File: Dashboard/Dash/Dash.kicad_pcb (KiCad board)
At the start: 2 copper layers, 184 x 75 mm, 44 parts, among them IC1 MCP25625-E_SS, J1 TACH-SERVO, J2 SPEED-SERVO, J4 UPPER Button, J6 LOWER Button, J7 DTF13-6P, U1 XIAO-ESP32-S3-SMD, U3 EA DOGM128W-6, Y1 ABM10AIG-16.000MHZ-4Z-T3

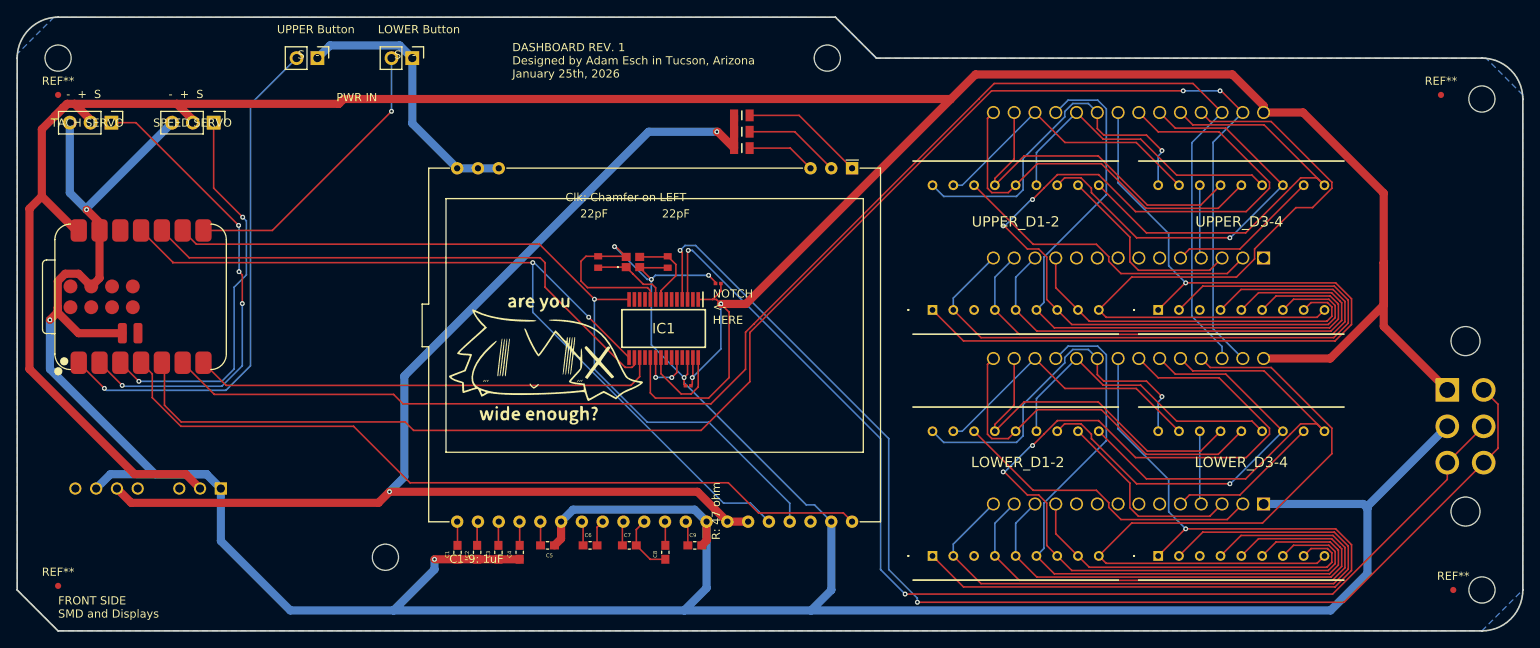
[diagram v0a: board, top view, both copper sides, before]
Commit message: Swapped upper button for CAN_INT
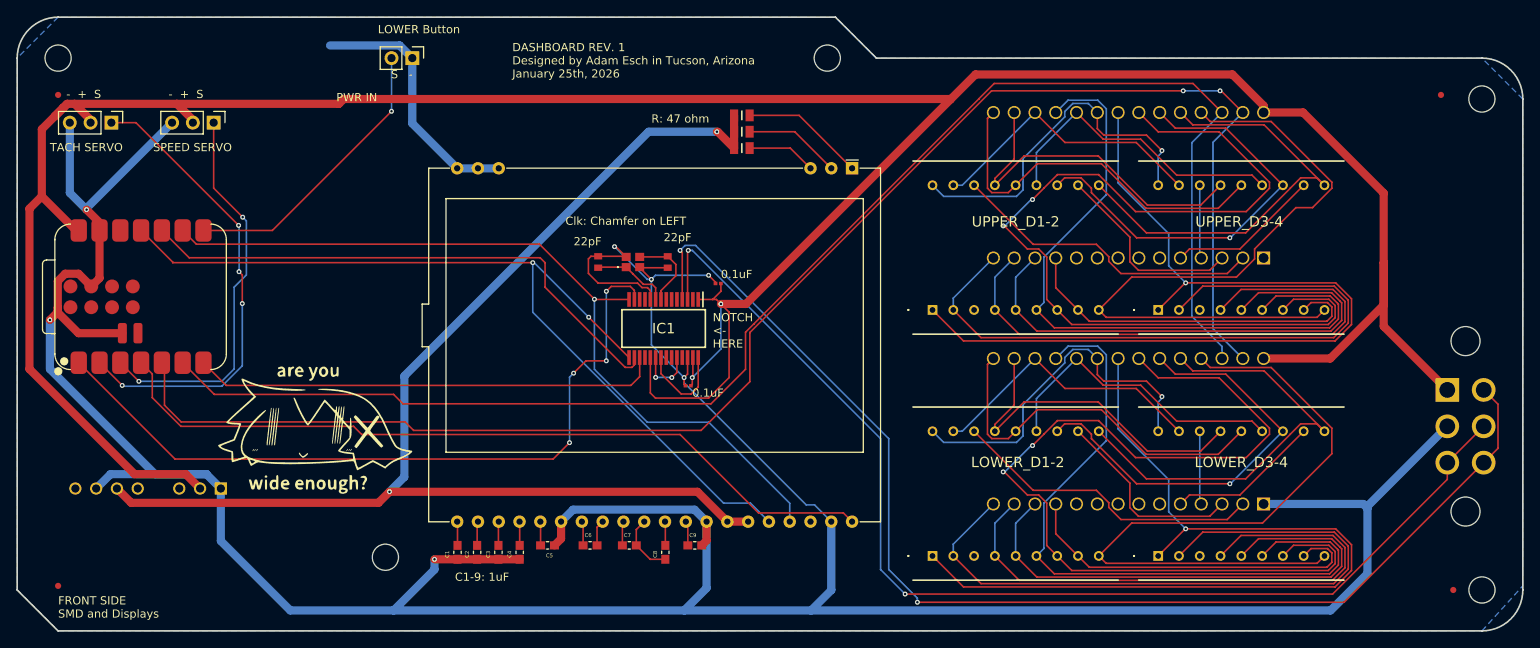
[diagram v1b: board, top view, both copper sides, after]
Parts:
- removed J4: UPPER Button, Connector_PinHeader_2.54mm:PinHeader_1x02_P2.54mm_Vertical
- moved G*** 29.4 mm to (86.0, 108.5)
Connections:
- IC1 pad 13: unconnected-(IC1-~{INT}-Pad13) -> CAN_INT
- U1 pad 1: UPPER_Button -> CAN_INT
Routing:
- net CAN_INT: track 0.00 -> 92.5 mm, vias 0 -> 4
- net UPPER_Button: track 63.6 -> 0.00 mm, vias 1 -> 0
- net GND: track 475.6 -> 471.2 mm
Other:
- board text added: "0.1uF"
- board text removed: "UPPER Button"

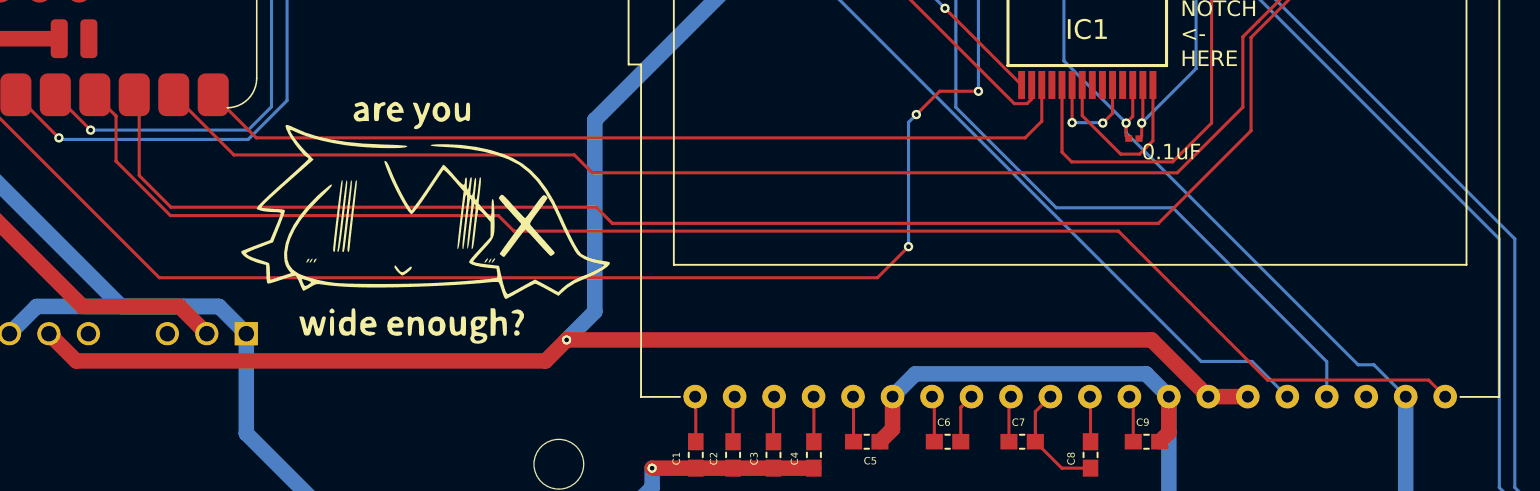
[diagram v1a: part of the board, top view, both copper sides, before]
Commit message: Cleanup on SPI/I2C Traces
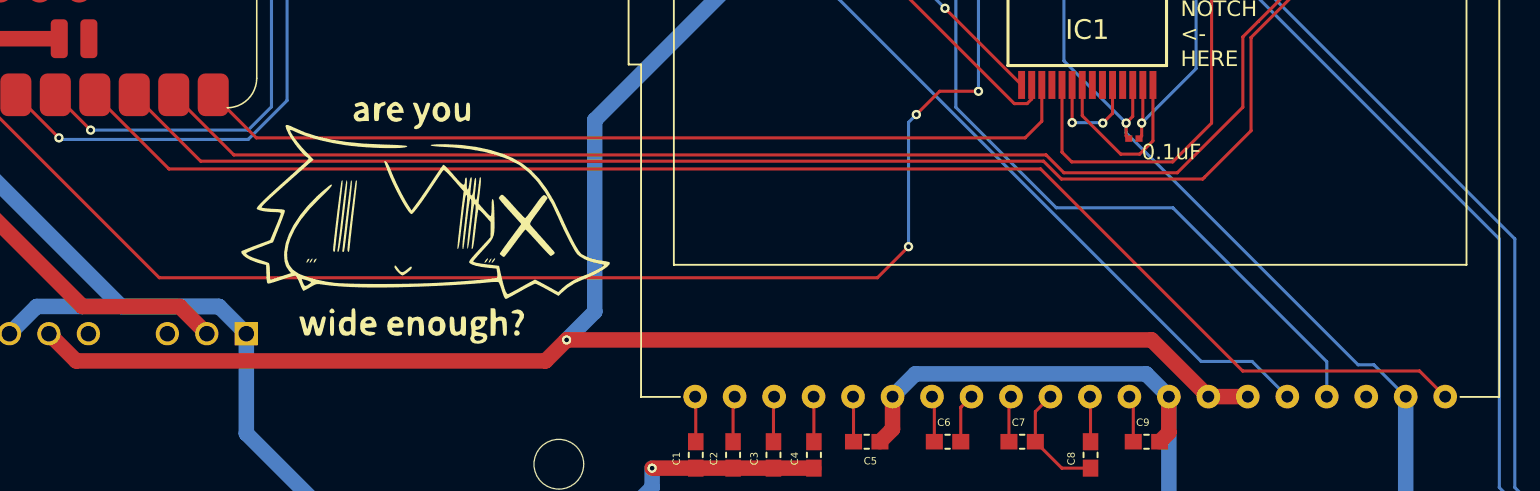
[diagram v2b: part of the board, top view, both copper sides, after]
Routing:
- net SDA: track 192.8 -> 188.0 mm
- net LCD_CS: track 96.6 -> 94.9 mm
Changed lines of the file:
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@@
 			(outputformat 1)
 			(mirror no)
-			(drillshape 1)
+			(drillshape 0)
 			(scaleselection 1)
 			(outputdirectory "")
@@
 	)
 	(segment
-		(start 169.399 66.101)
-		(end 193.693481 66.101)
+		(start 140.010481 95.502)
+		(end 167.510481 68.002)
 		(width 0.2)
 		(layer "F.Cu")
@@
 	)
 	(segment
-		(start 139.010481 101.026817)
-		(end 139.010481 96.5)
+		(start 127.5 105.246609)
+		(end 134.790689 105.246609)
 		(width 0.2)
 		(layer "F.Cu")
@@
 	)
 	(segment
-		(start 97.149057 105.246609)
-		(end 134.790689 105.246609)
+		(start 70.222481 100.228729)
+		(end 74.091304 104.097552)
 		(width 0.2)
 		(layer "F.Cu")
@@
 	)
 	(segment
-		(start 140.008481 95.502)
-		(end 140.010481 95.502)
+		(start 134.790689 105.246609)
+		(end 139.010481 101.026817)
 		(width 0.2)
 		(layer "F.Cu")
@@
 	)
 	(segment
-		(start 193.693481 66.101)
-		(end 197.240325 69.647844)
+		(start 126.350943 104.097552)
+		(end 127.5 105.246609)
 		(width 0.2)
 		(layer "F.Cu")
@@
 	)
 	(segment
-		(start 134.790689 105.246609)
-		(end 139.010481 101.026817)
+		(start 140.008481 95.502)
+		(end 140.010481 95.502)
 		(width 0.2)
 		(layer "F.Cu")
@@
 	)
 	(segment
-		(start 96 104.097552)
-		(end 97.149057 105.246609)
+		(start 74.091304 104.097552)
+		(end 126.350943 104.097552)
 		(width 0.2)
 		(layer "F.Cu")
@@
 	)
 	(segment
-		(start 139.010481 96.5)
-		(end 140.008481 95.502)
+		(start 193.693481 66.101)
+		(end 197.240325 69.647844)
 		(width 0.2)
 		(layer "F.Cu")
@@
 	)
 	(segment
-		(start 74.091304 104.097552)
-		(end 96 104.097552)
+		(start 169.399 66.101)
+		(end 193.693481 66.101)
 		(width 0.2)
 		(layer "F.Cu")
@@
 	)
 	(segment
-		(start 167.510481 67.989519)
-		(end 169.399 66.101)
+		(start 139.010481 96.5)
+		(end 140.008481 95.502)
 		(width 0.2)
 		(layer "F.Cu")
@@
 	)
 	(segment
-		(start 167.510481 68.002)
-		(end 167.510481 67.989519)
+		(start 167.510481 67.989519)
+		(end 169.399 66.101)
 		(width 0.2)
 		(layer "F.Cu")
@@
 	)
 	(segment
-		(start 70.222481 100.228729)
-		(end 74.091304 104.097552)
+		(start 139.010481 101.026817)
+		(end 139.010481 96.5)
 		(width 0.2)
 		(layer "F.Cu")
@@
 	)
 	(segment
-		(start 140.010481 95.502)
-		(end 167.510481 68.002)
+		(start 167.510481 68.002)
+		(end 167.510481 67.989519)
 		(width 0.2)
 		(layer "F.Cu")
@@
 	)
 	(segment
-		(start 68 105.422419)
-		(end 70.038791 107.46121)
-		(width 0.2)
-		(layer "F.Cu")
-		(net 11)
-	)
-	(segment
 		(start 197.132481 67)
 		(end 199.780325 69.647844)
@@
 	)
 	(segment
-		(start 98.443381 108.5)
-		(end 133.577581 108.5)
+		(start 139.538791 96.53879)
+		(end 139.540791 96.53879)
 		(width 0.2)
 		(layer "F.Cu")
@@
 	)
 	(segment
-		(start 70.038791 107.46121)
-		(end 97.404591 107.46121)
-		(width 0.2)
-		(layer "F.Cu")
-		(net 11)
-	)
-	(segment
-		(start 139.538791 96.53879)
-		(end 139.540791 96.53879)
+		(start 67.682481 100.228729)
+		(end 71.953752 104.5)
 		(width 0.2)
 		(layer "F.Cu")
@@
 	)
 	(segment
-		(start 68 100.546248)
-		(end 68 105.422419)
+		(start 127.3339 105.647609)
+		(end 136.429973 105.647609)
 		(width 0.2)
 		(layer "F.Cu")
@@
 	)
 	(segment
-		(start 133.577581 108.5)
+		(start 136.538791 105.538791)
 		(end 139.538791 102.53879)
 		(width 0.2)
@@
 	)
 	(segment
-		(start 97.404591 107.46121)
-		(end 98.443381 108.5)
+		(start 71.953752 104.5)
+		(end 126.186291 104.5)
 		(width 0.2)
 		(layer "F.Cu")
@@
 		(net 11)
 	)
+	(segment
+		(start 126.186291 104.5)
+		(end 127.3339 105.647609)
+		(width 0.2)
+		(layer "F.Cu")
+		(net 11)
+	)
+	(segment
+		(start 136.429973 105.647609)
+		(end 136.538791 105.538791)
+		(width 0.2)
+		(layer "F.Cu")
+		(net 11)
+	)
 	(via
 		(at 192.5 67)
@@
 	)
 	(segment
-		(start 150.967325 118.585109)
+		(start 150.382216 118)
 		(end 152.030325 119.648109)
 		(width 0.2)
@@
 	)
 	(segment
-		(start 65.142481 100.228729)
-		(end 66.510481 101.596729)
-		(width 0.2)
-		(layer "F.Cu")
-		(net 78)
-	)
-	(segment
-		(start 66.510481 101.596729)
-		(end 66.510481 104.5)
-		(width 0.2)
-		(layer "F.Cu")
-		(net 78)
-	)
-	(segment
-		(start 70.010481 108)
-		(end 91.111481 108)
+		(start 126 105)
+		(end 139 118)
 		(width 0.2)
 		(layer "F.Cu")
@@
 	)
 	(segment
-		(start 140.59559 118.585109)
-		(end 150.967325 118.585109)
-		(width 0.2)
-		(layer "F.Cu")
-		(net 78)
-	)
-	(segment
-		(start 92.111481 109)
-		(end 131.010482 109)
-		(width 0.2)
-		(layer "F.Cu")
-		(net 78)
-	)
-	(segment
-		(start 91.111481 108)
-		(end 92.111481 109)
+		(start 65.142481 100.228729)
+		(end 69.913752 105)
 		(width 0.2)
 		(layer "F.Cu")
@@
 	)
 	(segment
-		(start 66.510481 104.5)
-		(end 70.010481 108)
+		(start 139 118)
+		(end 150.382216 118)
 		(width 0.2)
 		(layer "F.Cu")
@@
 	)
 	(segment
-		(start 131.010482 109)
-		(end 140.59559 118.585109)
+		(start 69.913752 105)
+		(end 126 105)
 		(width 0.2)
 		(layer "F.Cu")
